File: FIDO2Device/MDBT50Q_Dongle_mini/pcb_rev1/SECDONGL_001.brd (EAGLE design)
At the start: 18 x 30 mm, 35 parts, among them CN1 CX60-24S-UNIT, CN2 IF_4PIN, CN3 IF_2PIN_SOL, CN4 IF_2PIN_SOL, SW1 SKRPACE010, SW2 SKTADAE010, U1 MDBT50Q-P1M, U2 MIC5323-3.3YMT-TR, X1 NX3215SA-32.768K-STD-MUA-9

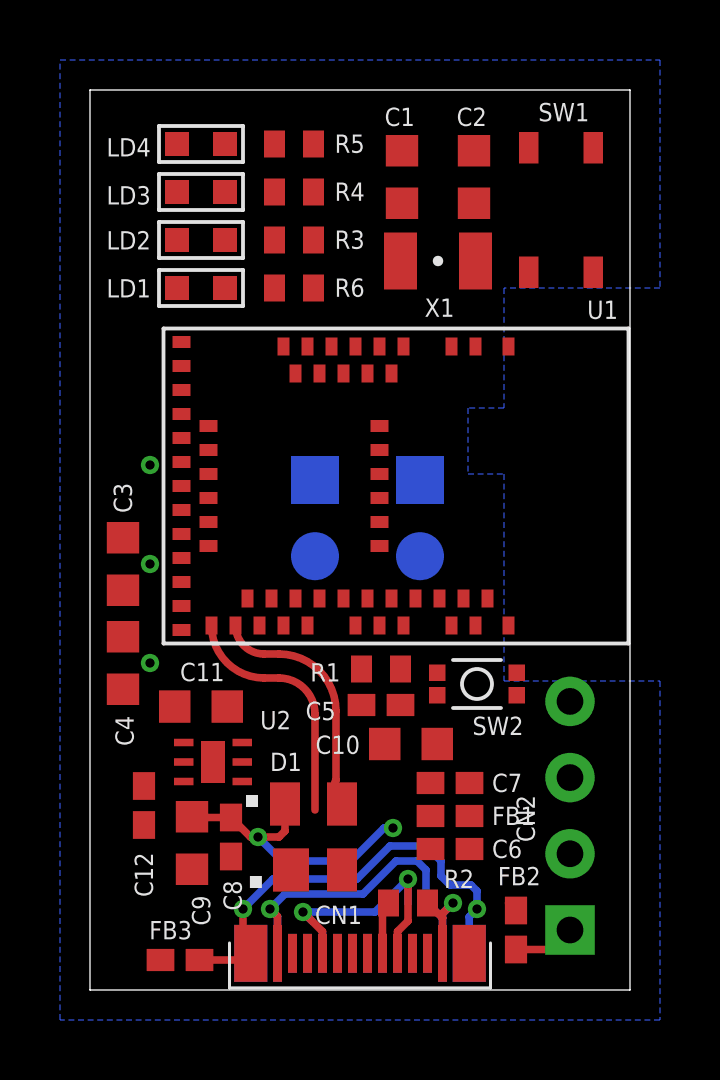
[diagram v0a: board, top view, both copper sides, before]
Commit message: 基板レイアウト作成
・配線がひと通り完了
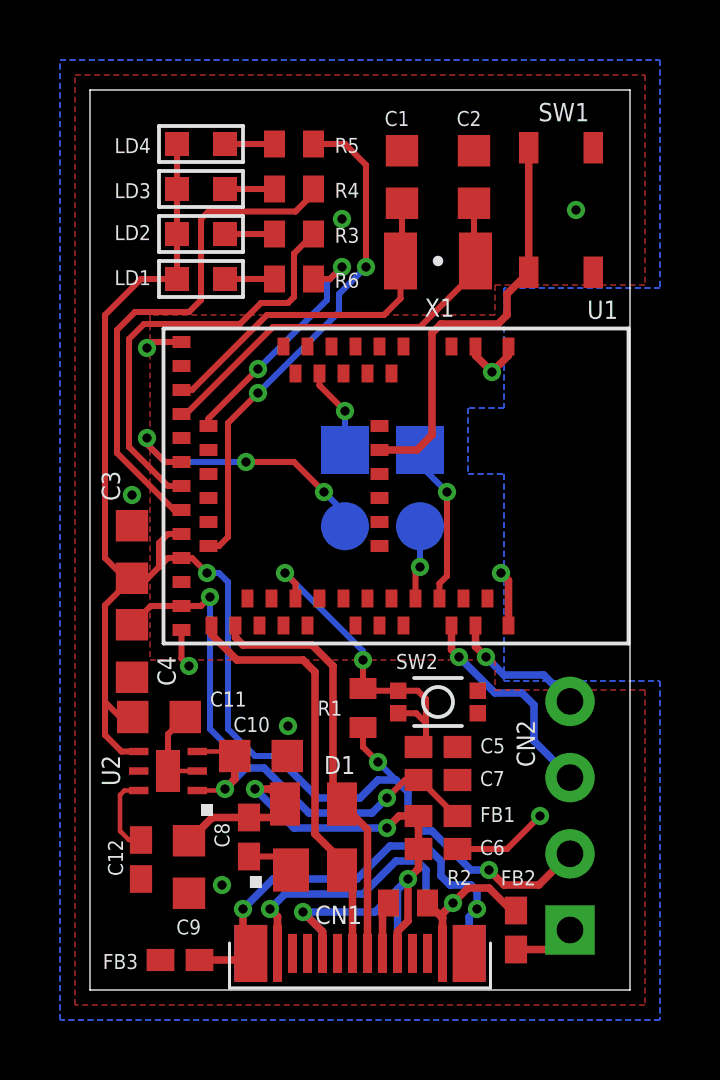
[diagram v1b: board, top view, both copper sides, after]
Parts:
- moved C10 5.02 mm to (5.70, 7.80)
- moved C5 2.36 mm to (11.6, 8.10), turned to 0 degrees
- moved C12 1.80 mm to (1.70, 4.35)
- moved U2 1.53 mm to (2.60, 7.30)
- moved C11 1.44 mm to (2.30, 9.10)
- moved SW2 1.43 mm to (11.6, 9.60)
- moved R1 1.43 mm to (9.10, 9.40), turned to 90 degrees
- moved CN3 1.41 mm to (8.50, 18.0)
- moved CN4 1.00 mm to (11.0, 18.0)
- moved C9 0.81 mm to (3.30, 4.10)
- moved C8 0.60 mm to (5.30, 5.10)
- moved C3 0.50 mm to (1.40, 14.6)
- moved C4 0.50 mm to (1.40, 11.3)
- moved C7 0.41 mm to (11.6, 7.00)
- moved C6 0.40 mm to (11.6, 4.70)
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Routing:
- net VDD_NRF: track 0.00 -> 52.3 mm, vias 2 -> 3
- net VBUS_NRF: track 0.00 -> 22.3 mm, vias 0 -> 3
- net LED3: track 0.00 -> 17.2 mm
- net LED4: track 0.00 -> 17.1 mm, vias 0 -> 2
- net 0V: track 2.07 -> 16.4 mm, vias 0 -> 9
- net LED2: track 0.00 -> 14.3 mm
- net XL2: track 0.00 -> 14.1 mm
- net SW1: track 0.00 -> 14.0 mm
- net XL1: track 0.00 -> 11.8 mm
- net RESET: track 0.00 -> 10.9 mm, vias 0 -> 2
- net TWI_SDA: track 0.22 -> 10.0 mm, vias 1 -> 3
- net LED1: track 0.00 -> 8.26 mm, vias 0 -> 2
- net SWDIO: track 0.00 -> 7.23 mm, vias 0 -> 1
- net D_P: track 8.02 -> 14.5 mm
- net D_N: track 7.87 -> 14.2 mm
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- added copper zone on layer 1, net 0V

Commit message: 基板レイアウト作成
・部品配置と配線を見直し
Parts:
- moved C9 5.69 mm to (6.50, 8.80), turned to 90 degrees
- moved U2 1.90 mm to (2.60, 5.40)
- moved C4 1.89 mm to (2.40, 9.70), turned to 0 degrees
- moved C12 1.86 mm to (1.90, 2.50)
- moved FB3 1.53 mm to (3.30, 2.50), turned to 270 degrees
- moved C10 1.28 mm to (4.90, 8.80), turned to 90 degrees
- moved C11 1.00 mm to (2.40, 8.10)
- moved R1 0.85 mm to (9.90, 9.70), turned to 270 degrees
- moved SW2 0.71 mm to (12.3, 9.70)
- moved FB2 0.32 mm to (14.1, 1.70)
- moved CN2 0.20 mm to (15.8, 2.00)
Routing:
- net VBUS_NRF: track 22.3 -> 31.7 mm, vias 3 -> 4
- net RESET: track 10.9 -> 12.5 mm
- net VDD_NRF: track 52.3 -> 50.8 mm, vias 3 -> 4
- net 0V: track 16.4 -> 17.9 mm, vias 9 -> 24
- net N$4: track 2.75 -> 1.71 mm
- net LED4: track 17.1 -> 16.3 mm
- net VBUS: track 25.8 -> 25.2 mm
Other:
- board text added: "GND"
- board text added: "PCLK"
- board text added: "PIO"
- board text added: "VDD"

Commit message: 回路図を修正
・定数を実際の使用部品と整合
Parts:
- C1, C2: value 9pF -> 12pF
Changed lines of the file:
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@@
 </autorouter>
 <elements>
-<element name="C1" library="Parts" package="C0603K" value="9pF" x="10.4" y="27.1" smashed="yes" rot="R90">
+<element name="C1" library="Parts" package="C0603K" value="12pF" x="10.4" y="27.1" smashed="yes" rot="R90">
 <attribute name="NAME" x="9.6" y="26.5" size="0.6" layer="25" rot="R90"/>
 <attribute name="VALUE" x="11.89125" y="26.3" size="0.7112" layer="27" rot="R90"/>
@@
 <attribute name="VALUE" x="0.529375" y="3.714375" size="0.7112" layer="27" rot="R270"/>
 </element>
-<element name="C2" library="Parts" package="C0603K" value="9pF" x="12.8" y="27.1" smashed="yes" rot="R90">
+<element name="C2" library="Parts" package="C0603K" value="12pF" x="12.8" y="27.1" smashed="yes" rot="R90">
 <attribute name="NAME" x="12" y="26.5" size="0.6" layer="25" rot="R90"/>
 <attribute name="VALUE" x="14.29125" y="26.3" size="0.7112" layer="27" rot="R90"/>
